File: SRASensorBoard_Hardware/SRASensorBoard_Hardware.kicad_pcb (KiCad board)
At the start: 2 copper layers, 124.6 x 91.3 mm, 41 parts, among them U1 Tive Header, U2 OKI, U3 OKI

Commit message: updated CCD connector
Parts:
- Conn5: value Molex_SL_03 -> Molex_SL_04; footprint MRDT_Connectors:MOLEX_SL_03_Horizontal -> MRDT_Connectors:MOLEX_SL_04_Horizontal
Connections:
- Conn5 pad 2: CCD_INT -> CCD_OS
- Conn5 pad 3: GND -> CCD_INT
- U1 pad PK3: (no net) -> CCD_OS
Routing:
- net CCD_OS: track 0.00 -> 68.9 mm
- net +3V3: track 23.6 -> 26.9 mm
- net CCD_INT: track 175.4 -> 174.1 mm
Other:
- board text added: "CCD_OS"

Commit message: added CCD connector
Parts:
- Conn5: value Molex_SL_04 -> Molex_SL_05; footprint MRDT_Connectors:MOLEX_SL_04_Horizontal -> MRDT_Connectors:MOLEX_SL_05_Horizontal
- moved Conn5 7.73 mm to (181.3, 50.9)
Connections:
- Conn5 pad 2: CCD_OS -> CCD_INT2
- Conn5 pad 3: CCD_INT -> CCD_INT1
- Conn5 pad 4: GND -> CCD_OS
- U1 pad PA4: (no net) -> Net-(U1-PadPA4)
- U1 pad PA5: (no net) -> Net-(U1-PadPA5)
- U1 pad PA6: (no net) -> Net-(U1-PadPA6)
- U1 pad PA7: (no net) -> Net-(U1-PadPA7)
- U1 pad PB2: (no net) -> Net-(U1-PadPB2)
- U1 pad PB3: (no net) -> Net-(U1-PadPB3)
- U1 pad PB4: (no net) -> Net-(U1-PadPB4)
- U1 pad PC4: (no net) -> Net-(U1-PadPC4)
- U1 pad PC5: (no net) -> Net-(U1-PadPC5)
- U1 pad PC6: (no net) -> Net-(U1-PadPC6)
- U1 pad PC7: (no net) -> Net-(U1-PadPC7)
- U1 pad PD0: (no net) -> Net-(U1-PadPD0)
- U1 pad PD1: (no net) -> AnalogOut
- U1 pad PD2: (no net) -> Net-(U1-PadPD2)
- U1 pad PD3: (no net) -> Net-(U1-PadPD3)
- U1 pad PD4: (no net) -> Net-(U1-PadPD4)
- U1 pad PD5: (no net) -> Net-(U1-PadPD5)
- U1 pad PD7: (no net) -> Net-(U1-PadPD7)
- U1 pad PE0: CCD_INT -> CCD_INT1
- U1 pad PE1: (no net) -> CCD_INT2
- U1 pad PE3: (no net) -> Net-(U1-PadPE3)
- U1 pad PE4: (no net) -> Net-(U1-PadPE4)
- U1 pad PF1: (no net) -> Net-(U1-PadPF1)
- U1 pad PF2: (no net) -> Net-(U1-PadPF2)
- U1 pad PF3: (no net) -> Net-(U1-PadPF3)
- U1 pad PG0: (no net) -> Net-(U1-PadPG0)
- U1 pad PG1: (no net) -> Net-(U1-PadPG1)
- U1 pad PH0: (no net) -> Net-(U1-PadPH0)
- U1 pad PH1: (no net) -> Net-(U1-PadPH1)
- U1 pad PH2: (no net) -> Net-(U1-PadPH2)
- U1 pad PH3: (no net) -> Net-(U1-PadPH3)
- U1 pad PK0: (no net) -> Net-(U1-PadPK0)
- U1 pad PK1: (no net) -> Net-(U1-PadPK1)
- U1 pad PK2: (no net) -> Net-(U1-PadPK2)
- U1 pad PK4: (no net) -> Net-(U1-PadPK4)
- U1 pad PK5: (no net) -> Net-(U1-PadPK5)
- U1 pad PK6: (no net) -> Net-(U1-PadPK6)
- U1 pad PK7: (no net) -> Net-(U1-PadPK7)
- U1 pad PL0: (no net) -> Net-(U1-PadPL0)
- U1 pad PL1: (no net) -> Net-(U1-PadPL1)
- U1 pad PL2: (no net) -> Net-(U1-PadPL2)
- U1 pad PL3: (no net) -> Net-(U1-PadPL3)
- U1 pad PL4: (no net) -> Net-(U1-PadPL4)
- U1 pad PL5: (no net) -> Net-(U1-PadPL5)
- U1 pad PM0: (no net) -> Net-(U1-PadPM0)
- U1 pad PM1: (no net) -> Net-(U1-PadPM1)
- U1 pad PM2: (no net) -> Net-(U1-PadPM2)
- U1 pad PM3: (no net) -> Net-(U1-PadPM3)
- U1 pad PM4: (no net) -> Net-(U1-PadPM4)
- U1 pad PM5: (no net) -> Net-(U1-PadPM5)
- U1 pad PM6: (no net) -> Net-(U1-PadPM6)
- U1 pad PM7: (no net) -> Net-(U1-PadPM7)
- U1 pad PN3: (no net) -> Net-(U1-PadPN3)
- U1 pad PP0: (no net) -> Net-(U1-PadPP0)
- U1 pad PP1: (no net) -> Net-(U1-PadPP1)
- U1 pad PP2: (no net) -> Net-(U1-PadPP2)
- U1 pad PP3: (no net) -> Net-(U1-PadPP3)
- U1 pad PQ0: (no net) -> Net-(U1-PadPQ0)
- U1 pad PQ1: (no net) -> Net-(U1-PadPQ1)
- U1 pad PQ2: (no net) -> Net-(U1-PadPQ2)
- U1 pad PQ3: (no net) -> Net-(U1-PadPQ3)

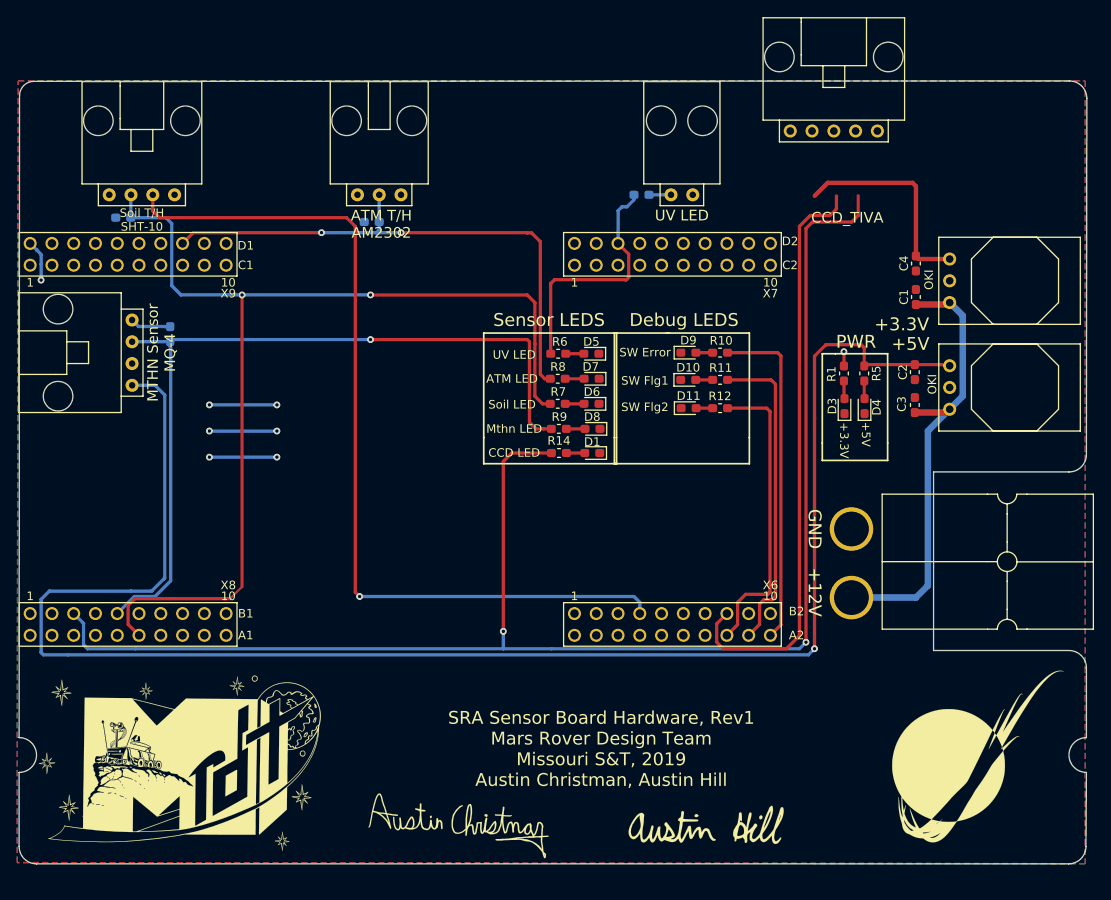
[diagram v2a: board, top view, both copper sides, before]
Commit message: Wired CCD
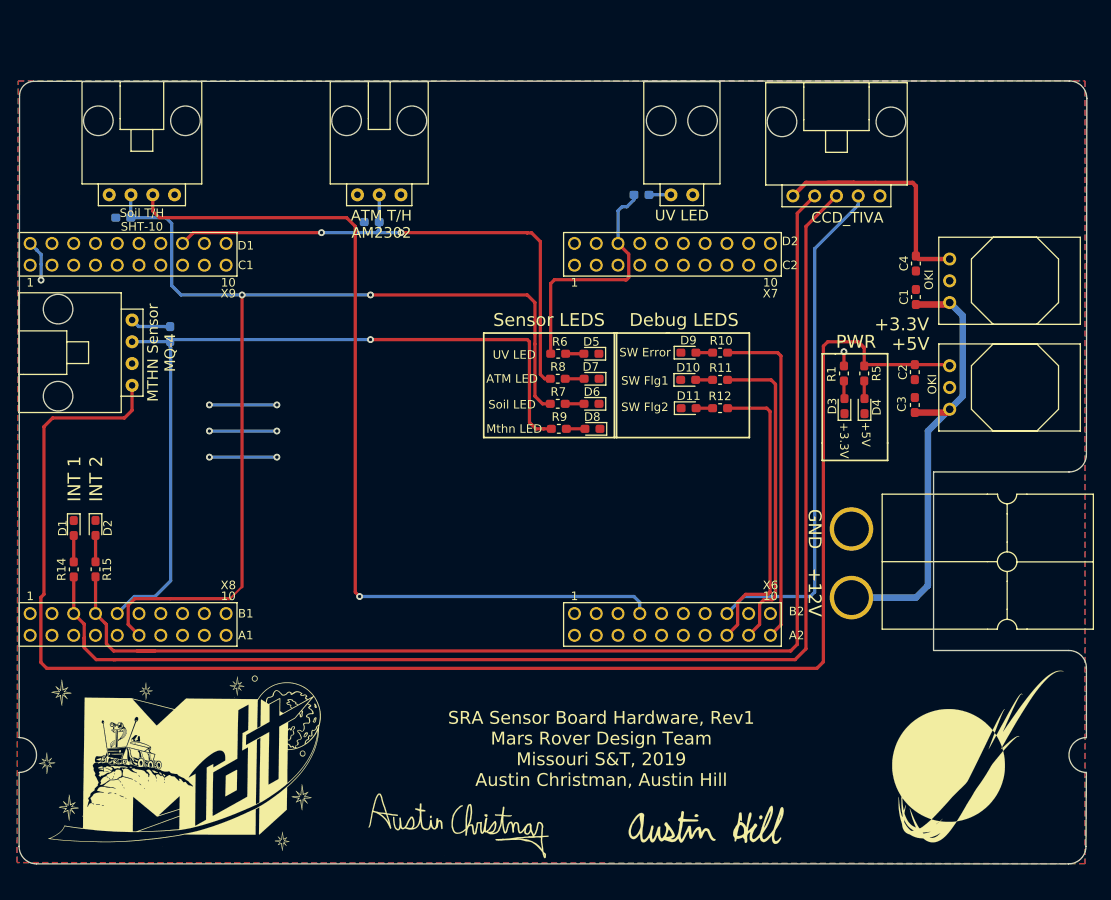
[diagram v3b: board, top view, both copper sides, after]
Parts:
- added D2: LED, Diode_SMD:D_0603_1608Metric_Pad1.05x0.95mm_HandSolder, F.Cu at (95.2, 97.2)
- added R15: 500, Resistor_SMD:R_0603_1608Metric_Pad1.05x0.95mm_HandSolder, F.Cu at (95.2, 102.0)
- moved D1 61.1 mm to (92.6, 97.2), turned to 270 degrees
- moved R14 58.2 mm to (92.6, 102.0), turned to 90 degrees
- moved Conn5 7.58 mm to (181.6, 58.4)
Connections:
- net AnalogOut renamed Net-(U1-PadPD1)
- R14 pad 1: CCD_INT -> CCD_INT1
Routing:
- net CCD_INT: track 174.1 -> 0.00 mm, vias 2 -> 0
- net CCD_INT1: track 0.00 -> 149.5 mm
- net CCD_INT2: track 0.00 -> 144.8 mm
- net CCD_OS: track 68.9 -> 59.6 mm
- net +3V3: track 26.9 -> 32.5 mm
- net Net-(D2-Pad2): track 0.00 -> 3.08 mm
- net +5V: track 191.5 -> 188.7 mm, vias 1 -> 0
- net Net-(D1-Pad2): track 2.14 -> 3.08 mm
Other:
- board text added: "CCD_INT1"
- board text added: "CCD_INT2"
- board text added: "INT 1"
- board text added: "INT 2"
- board text removed: "CCD LED"
- board text removed: "CCD_INT"

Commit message: created Gerbs
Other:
- board text added: "SRA Sensor Board Hardware, Rev2 Mars Rover Design Team Missouri S&T, 2019 Austin Christman, Austin Hill"
- board text removed: "SRA Sensor Board Hardware, Rev1 Mars Rover Design Team Missouri S&T, 2019 Austin Christman, Austin Hill"
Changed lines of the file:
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@@
   )
   (setup
-    (last_trace_width 0.381)
+    (last_trace_width 0.25)
     (user_trace_width 0.381)
     (user_trace_width 0.508)
@@
     (effects (font (size 0.992 0.992) (thickness 0.248)) (justify mirror))
   )
-  (gr_text "SRA Sensor Board Hardware, Rev1\nMars Rover Design Team\nMissouri S&T, 2019\nAustin Christman, Austin Hill" (at 154.178 122.936) (layer F.SilkS)
+  (gr_text "SRA Sensor Board Hardware, Rev2\nMars Rover Design Team\nMissouri S&T, 2019\nAustin Christman, Austin Hill" (at 154.178 122.936) (layer F.SilkS)
     (effects (font (size 1.5 1.5) (thickness 0.3)))
   )

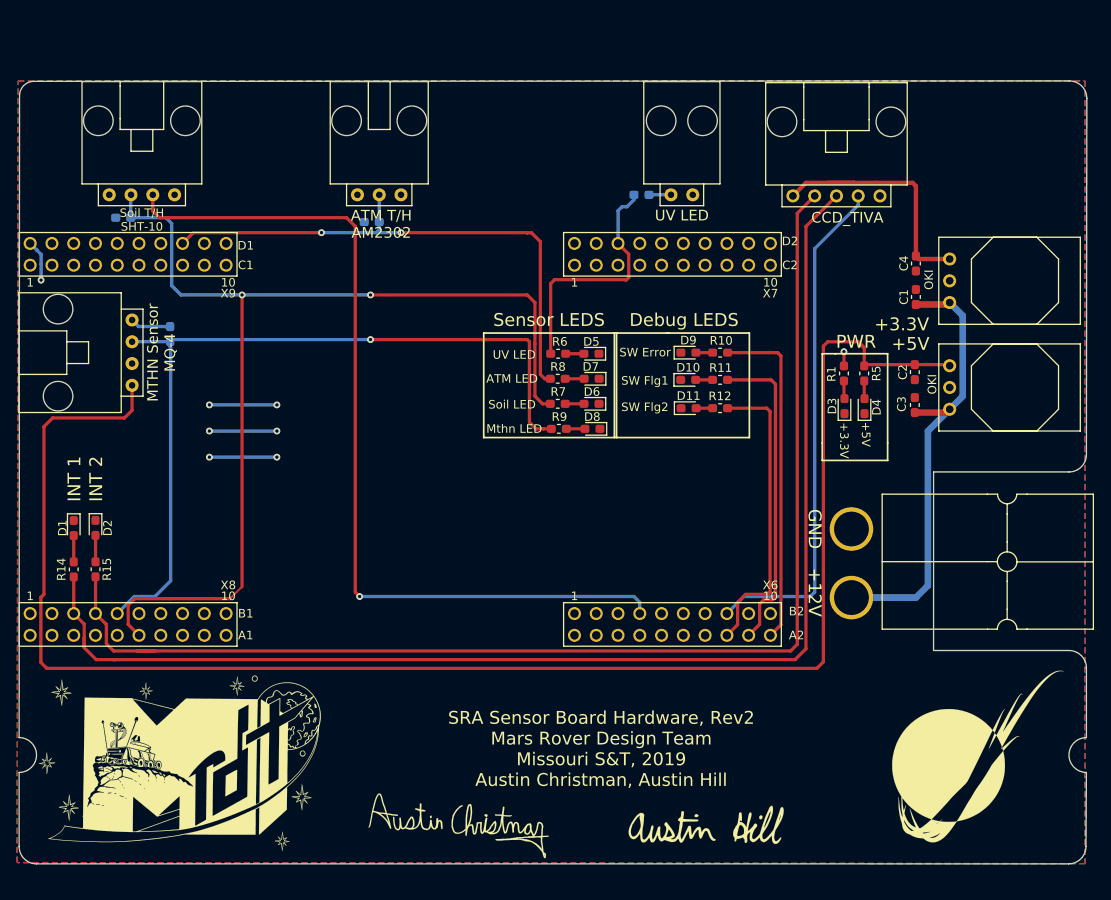
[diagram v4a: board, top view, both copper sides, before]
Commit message: Rev 2 rework
Changed the connectors to vertical, retraced traces, etc.
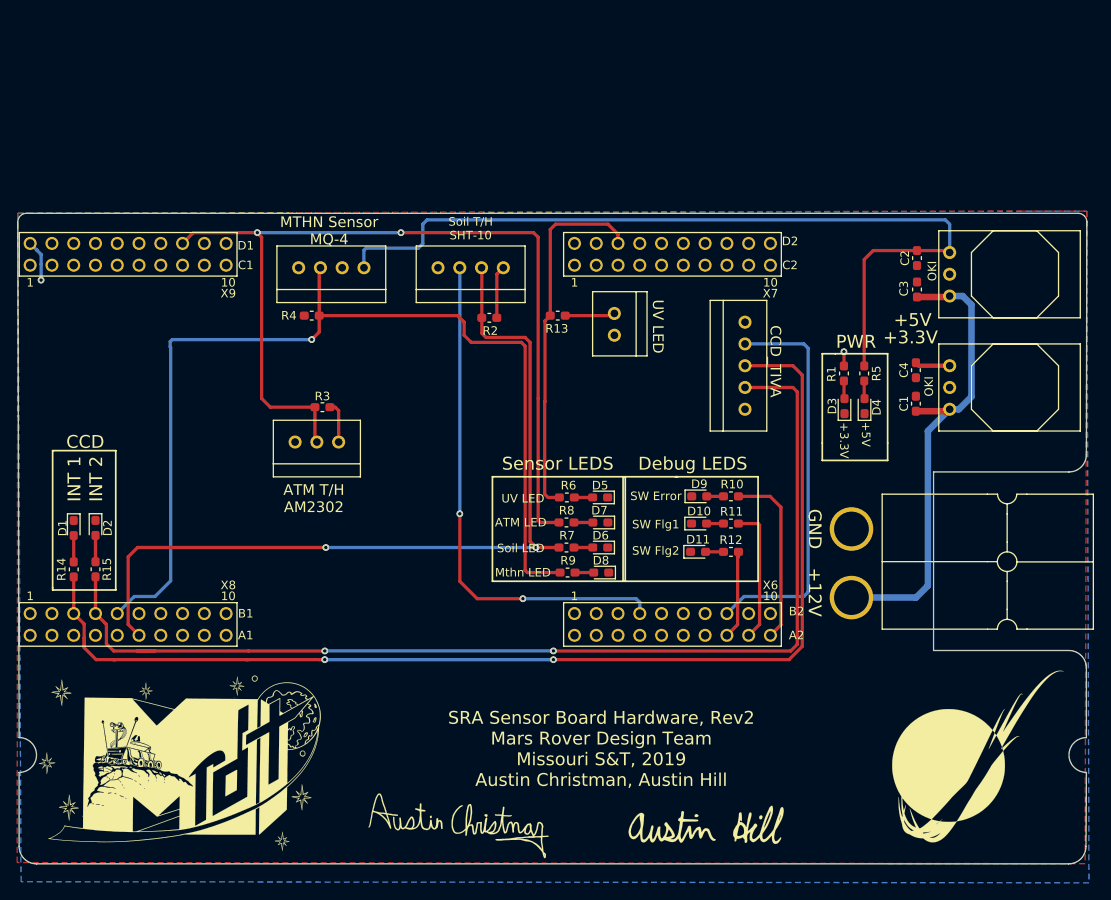
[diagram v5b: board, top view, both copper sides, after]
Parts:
- Conn2, Conn4: footprint MRDT_Connectors:MOLEX_SL_04_Horizontal -> MRDT_Connectors:MOLEX_SL_04_Vertical
- Conn3: footprint MRDT_Connectors:MOLEX_SL_03_Horizontal -> MRDT_Connectors:MOLEX_SL_03_Vertical
- Conn5: footprint MRDT_Connectors:MOLEX_SL_05_Horizontal -> MRDT_Connectors:MOLEX_SL_05_Vertical
- Conn6: footprint MRDT_Connectors:MOLEX_SL_02_Horizontal -> MRDT_Connectors:MOLEX_SL_02_Vertical
- R13, R2, R3, R4: moved to F.Cu
- moved R2 44.3 mm to (141.1, 72.6), turned to 180 degrees
- moved Conn2 39.3 mm to (138.9, 66.8), turned to 180 degrees
- moved Conn3 31.5 mm to (126.1, 89.7), turned to 180 degrees
- moved Conn4 25.3 mm to (122.7, 66.8), turned to 180 degrees
- moved Conn5 22.5 mm to (170.9, 78.2), turned to 90 degrees
- moved R3 22.4 mm to (121.6, 83.1), turned to 180 degrees
- moved R13 17.1 mm to (149.1, 72.4)
- moved Conn6 17.0 mm to (155.7, 73.4), turned to 270 degrees
- moved D10 16.8 mm to (165.6, 96.6)
- moved R11 16.8 mm to (169.3, 96.6)
- moved D9 16.8 mm to (165.6, 93.5)
- moved R10 16.8 mm to (169.3, 93.5)
- moved R12 16.8 mm to (169.3, 99.9)
- moved D5 16.8 mm to (154.0, 93.6)
- moved R6 16.8 mm to (150.2, 93.6)
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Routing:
- net +5V: track 188.7 -> 99.8 mm
- net Soil_Sck: track 103.9 -> 59.9 mm, vias 1 -> 2
- net Atm_Dout: track 64.2 -> 108.1 mm
- net GND: track 33.2 -> 4.85 mm, vias 7 -> 1
- net SW_Flag2: track 34.8 -> 10.3 mm
- net Soil_Data: track 123.6 -> 99.1 mm
- net Methane_Vout: track 94.7 -> 117.9 mm
- net SW_Flag1: track 37.0 -> 16.1 mm
- net SW_ERROR: track 39.5 -> 20.9 mm
- net CCD_INT2: track 144.8 -> 127.7 mm, vias 0 -> 2
- net CCD_INT1: track 149.5 -> 133.9 mm, vias 0 -> 2
- net +3V3: track 32.5 -> 17.0 mm
- net UV_TOGGLE: track 29.6 -> 43.3 mm
- net CCD_OS: track 59.6 -> 46.5 mm
- net Net-(C1-Pad1): track 53.8 -> 56.9 mm
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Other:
- board size 124.6 x 91.3 mm -> 124.7 x 75.9 mm
- board text added: "1 2 3"
- board text added: "1 2 3 4"
- board text added: "5 4 3 2 1"
- board text added: "CCD"
- board text removed: "3 2 1"
- board text removed: "4 3 2 1"
